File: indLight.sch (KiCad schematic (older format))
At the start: 35 parts, among them P1 TTL_232R_3V3, P2 CONN_01X02, P3 CONN_01X03, P4 CONN_01X03, U1 LM317EMPX, U2 MAX5035E, U3 SN74LVC2G17, U4 esp8266_esp-02

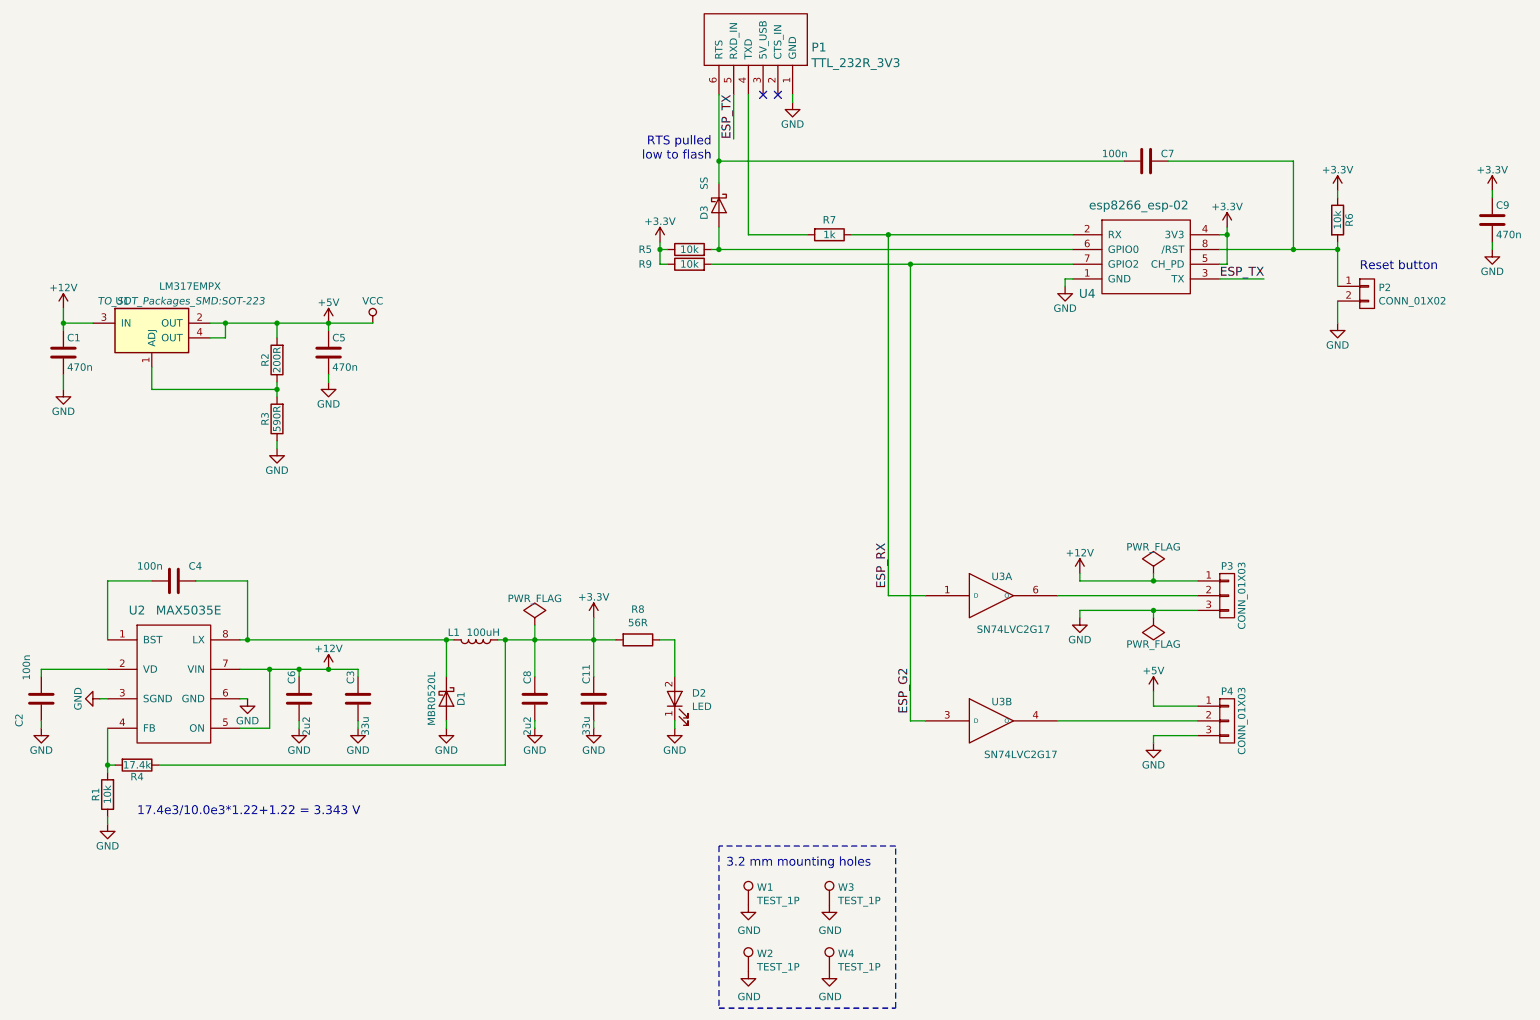
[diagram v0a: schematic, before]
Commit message: REV1. Added top lid, better DCDC, gerb. Ordered
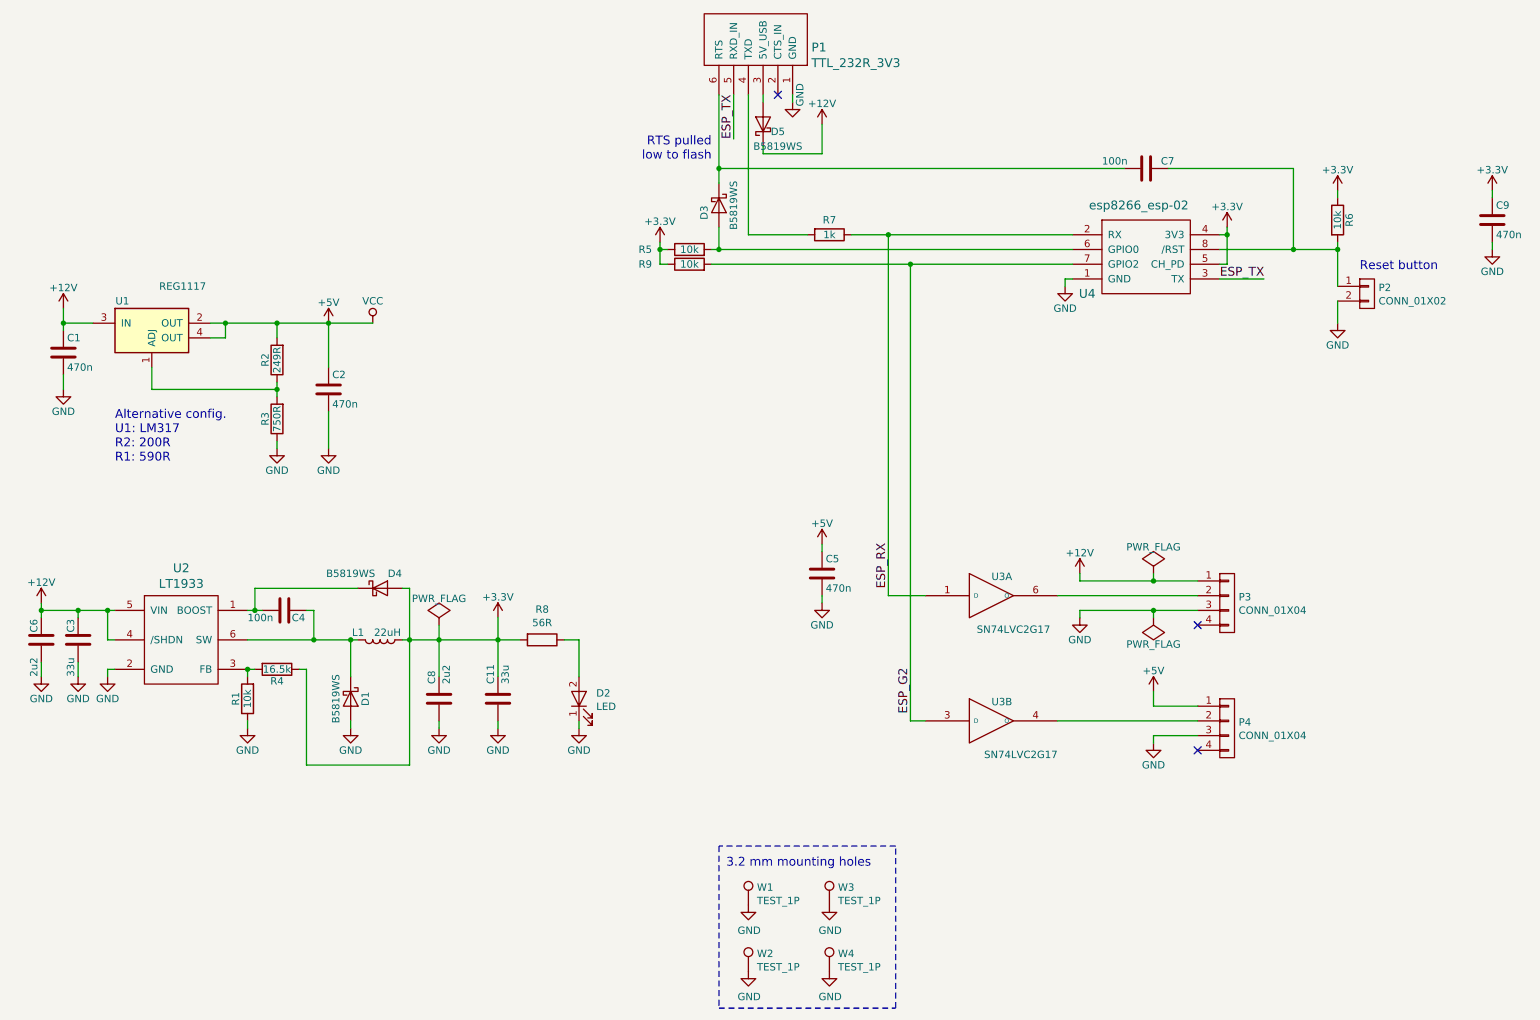
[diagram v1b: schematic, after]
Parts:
- removed P3, P4: CONN_01X03, Socket_Strips:Socket_Strip_Straight_1x03, symbol CONN_01X03
- removed U2: MAX5035E, Housings_SOIC:SOIC-8_3.9x4.9mm_Pitch1.27mm, symbol MAX5035E
- added D4, D5: B5819WS, Diodes_SMD:D_SOD-323_HandSoldering, symbol D_Schottky
- added P3, P4: CONN_01X04, Socket_Strips:Socket_Strip_Straight_1x04, symbol CONN_01X04
- added U2: LT1933, TO_SOT_Packages_SMD:SOT-23-6_Handsoldering, symbol LT1933
- C2: value 100n -> 470n
- D1: value MBR0520L -> B5819WS; footprint Diodes_SMD:SOD-123 -> Diodes_SMD:D_SOD-323_HandSoldering
- D3: value SS -> B5819WS; footprint Diodes_SMD:SOD-123 -> Diodes_SMD:D_SOD-323_HandSoldering
- L1: value 100uH -> 22uH; footprint myStuff:cc_5022 -> myStuff:DO1608
- R2: value 200R -> 249R
- R3: value 590R -> 750R
- R4: value 17.4k -> 16.5k
- U1: value LM317EMPX -> REG1117; footprint TO_SOT_Packages_SMD:SOT-223 -> myStuff:SOT-223
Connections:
- net +12V: now also D5.1 (K), P3.1 (P1), U2.4 (/SHDN), U2.5 (VIN)
- net +3V3: now also D4.2 (A)
- net +5V: now also C2.1, P4.1 (P1)
- net GND: now also C2.2, P3.3 (P3), P4.3 (P3), U2.2 (GND); no longer C2.1
- net at U3.6 (O): now also P3.2 (P2)
- net at U3.4 (O): now also P4.2 (P2)
- net at C4.2: now also D4.1 (K), U2.1 (BOOST)
- net at R1.2, R4.2: now also U2.3 (FB)
- net at C4.1, D1.1 (K), L1.2: now also U2.6 (SW)
- net at P1.3 (5V_USB): now also D5.2 (A)
- no-connect marks 2 -> 3
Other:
- note added: "Alternative config.\nU1: LM317\nR2: 200R\nR1: 590R"
- note removed: "17.4e3/10.0e3*1.22+1.22 = 3.343 V"
- moved on the sheet: C11, C3, C4, C5, C6, C7, C8, D1, D2, L1, R1, R4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
